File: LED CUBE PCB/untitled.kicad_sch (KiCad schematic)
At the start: 42 parts, among them J1 Conn_01x06, J3 Conn_01x09, SW1 BZCN_TSA007A1518B03, U1 TPS7A2633DRVR, U2 CH340C, Y3 8MHz, Y4 32.786KHz

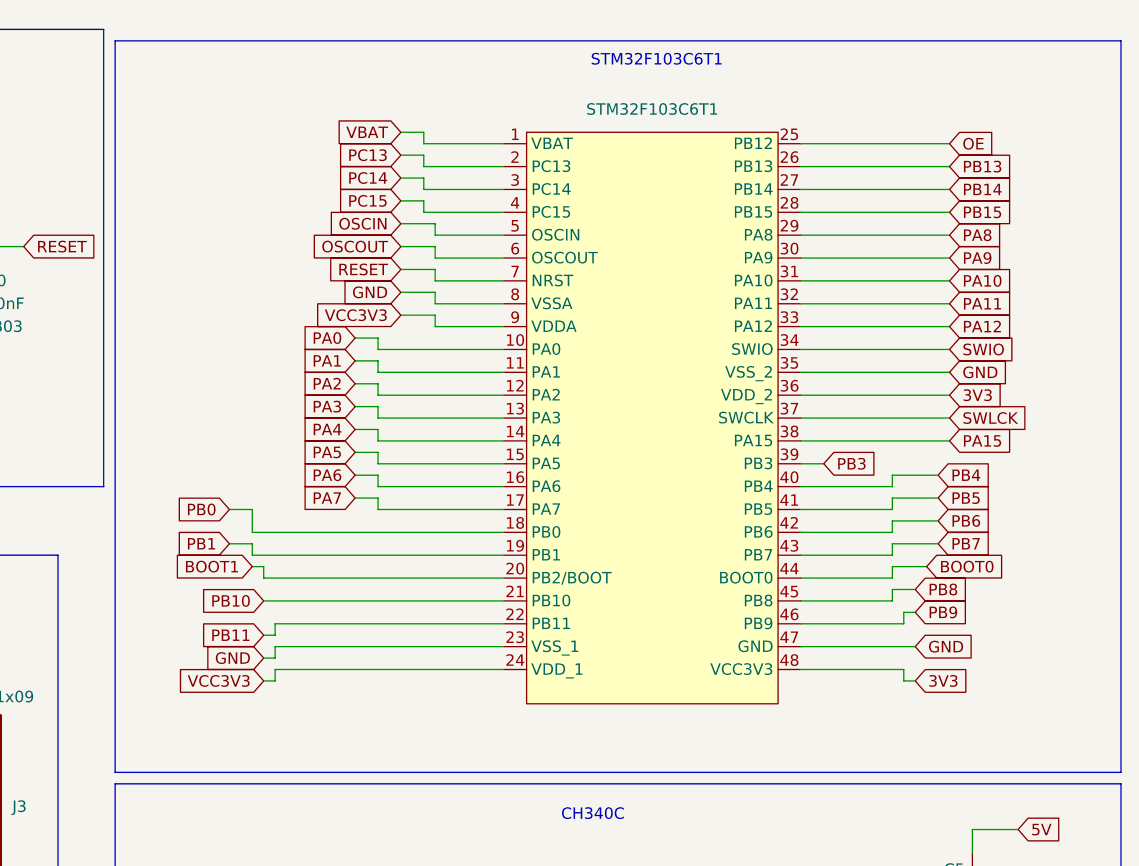
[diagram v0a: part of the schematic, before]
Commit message: Replaced symbol for TXB and STM
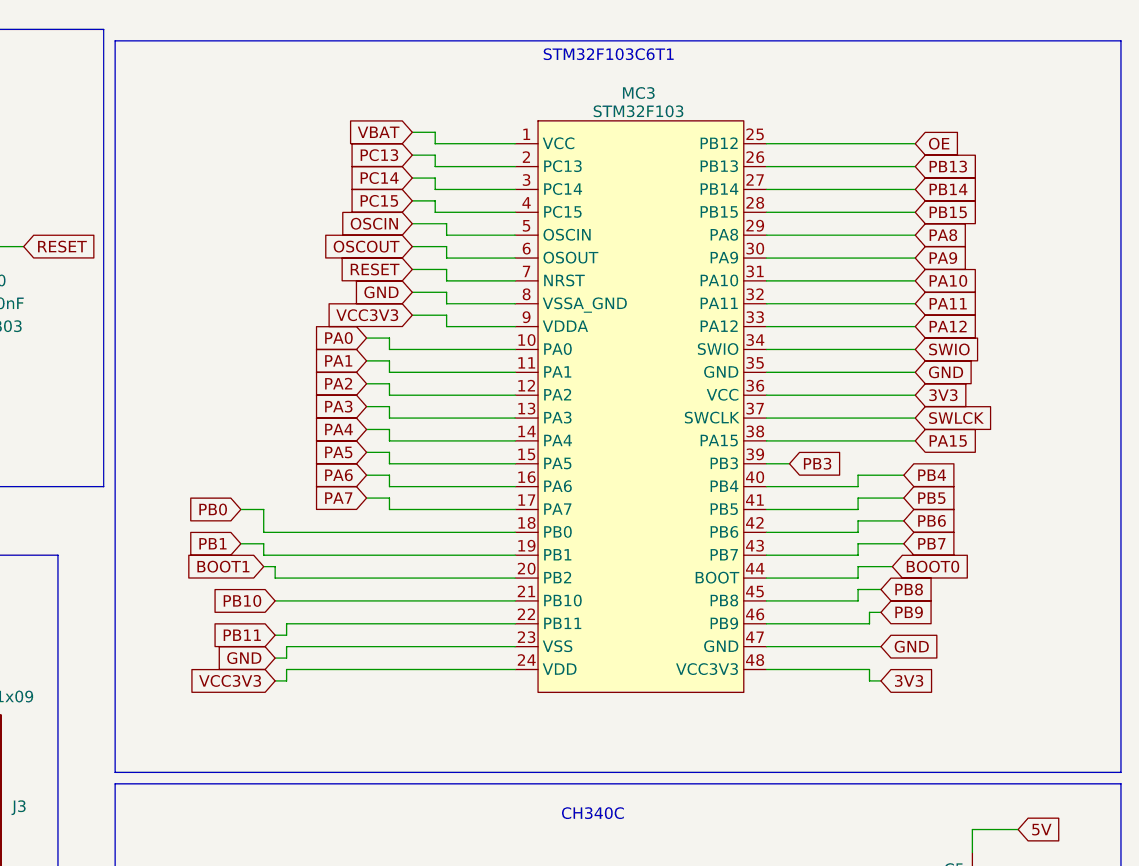
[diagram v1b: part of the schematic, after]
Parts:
- removed STM32F103C6T1: ~, Borna KiCAD Library:TQFP48, symbol STM32F103C6:STM32F103C6
- added MC3: STM32F103, symbol STM32F103c:STM32F103
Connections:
- net 3V3: now also MC3.36 (VCC), MC3.48 (VCC3V3)
- net BOOT0: now also MC3.44 (BOOT)
- net BOOT1: now also MC3.20 (PB2)
- net DN: now also MC3.32 (PA11)
- net DP: now also MC3.33 (PA12)
- net GND: now also MC3.23 (VSS), MC3.35 (GND), MC3.47 (GND), MC3.8 (VSSA_GND)
- net OE: now also MC3.25 (PB12)
- net OSCIN: now also MC3.5 (OSCIN)
- net OSCOUT: now also MC3.6 (OSOUT)
- net PA0: now also MC3.10 (PA0)
- net PA1: now also MC3.11 (PA1)
- net PA10: now also MC3.31 (PA10)
- net PA15: now also MC3.38 (PA15)
- net PA2: now also MC3.12 (PA2)
- net PA3: now also MC3.13 (PA3)
- net PA4: now also MC3.14 (PA4)
- net PA5: now also MC3.15 (PA5)
- net PA6: now also MC3.16 (PA6)
- net PA7: now also MC3.17 (PA7)
- net PA8: now also MC3.29 (PA8)
- net PA9: now also MC3.30 (PA9)
- net PB0: now also MC3.18 (PB0)
- net PB1: now also MC3.19 (PB1)
- net PB10: now also MC3.21 (PB10)
- net PB11: now also MC3.22 (PB11)
- net PB13: now also MC3.26 (PB13)
- net PB14: now also MC3.27 (PB14)
- net PB15: now also MC3.28 (PB15)
- net PB3: now also MC3.39 (PB3)
- net PB4: now also MC3.40 (PB4)
- net PB5: now also MC3.41 (PB5)
- net PB6: now also MC3.42 (PB6)
- net PB7: now also MC3.43 (PB7)
- net PB8: now also MC3.45 (PB8)
- net PB9: now also MC3.46 (PB9)
- net PC13: now also MC3.2 (PC13)
- net PC14: now also MC3.3 (PC14)
- net PC15: now also MC3.4 (PC15)
- net RESET: now also MC3.7 (NRST)
- net SWIO: now also MC3.34 (SWIO)
- net SWLCK: now also MC3.37 (SWCLK)
- net VBAT: now also MC3.1 (VCC)
- net VCC3V3: now also MC3.24 (VDD), MC3.9 (VDDA)

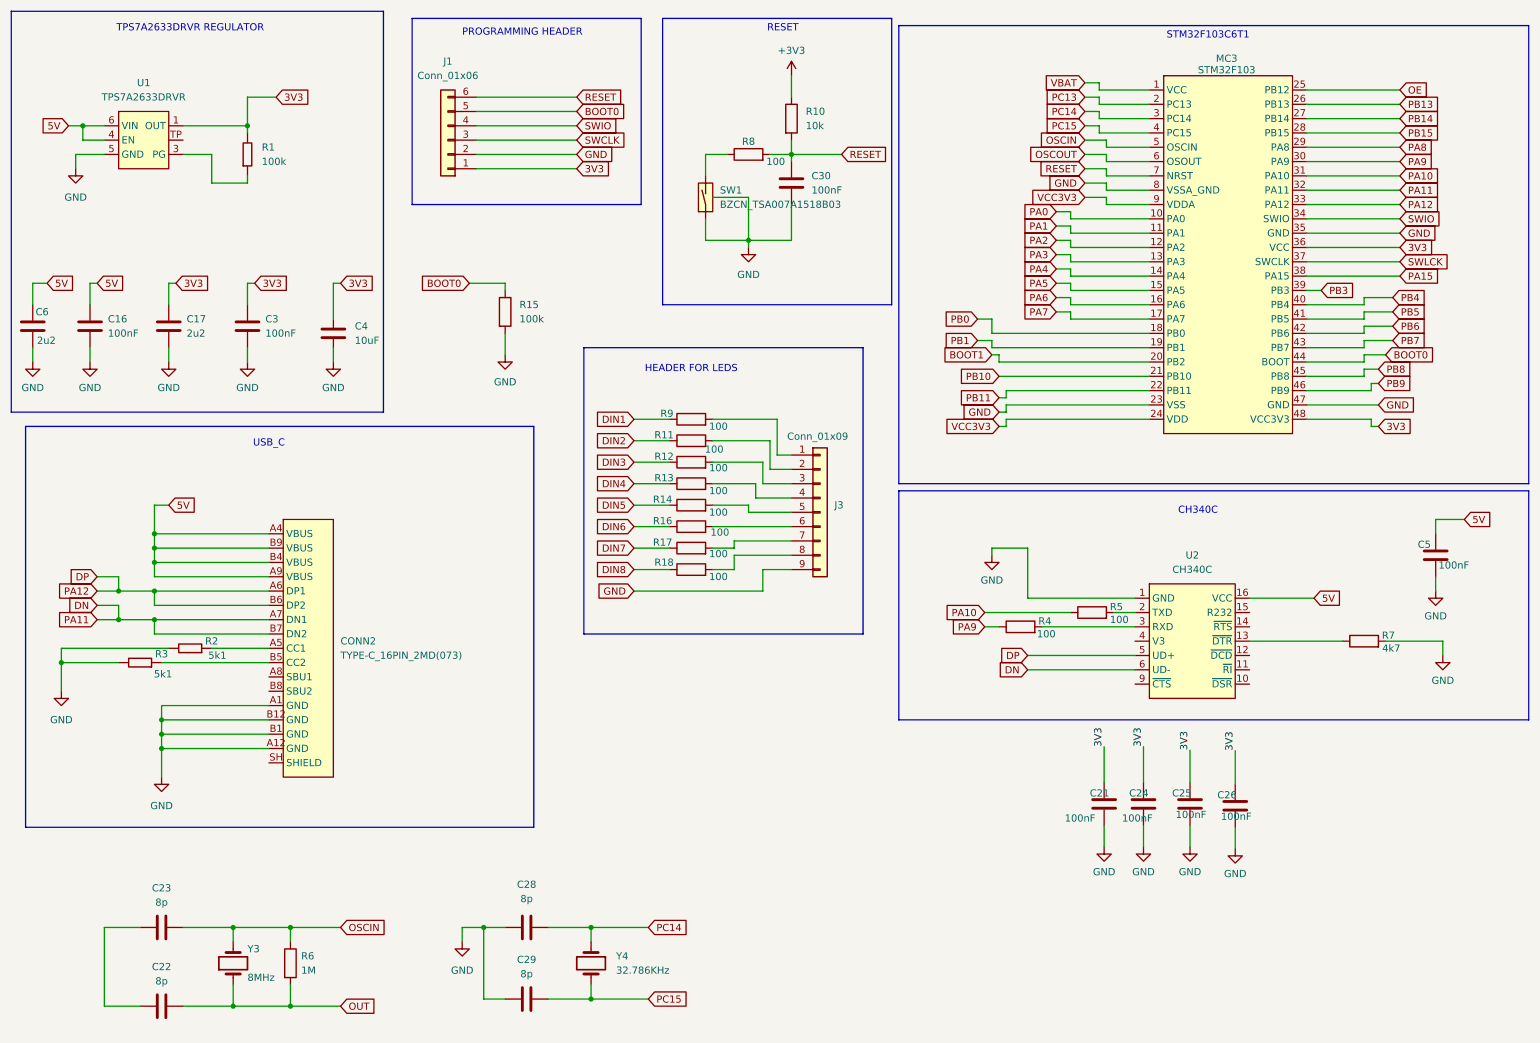
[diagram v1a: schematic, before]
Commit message: Added fuse and bat20
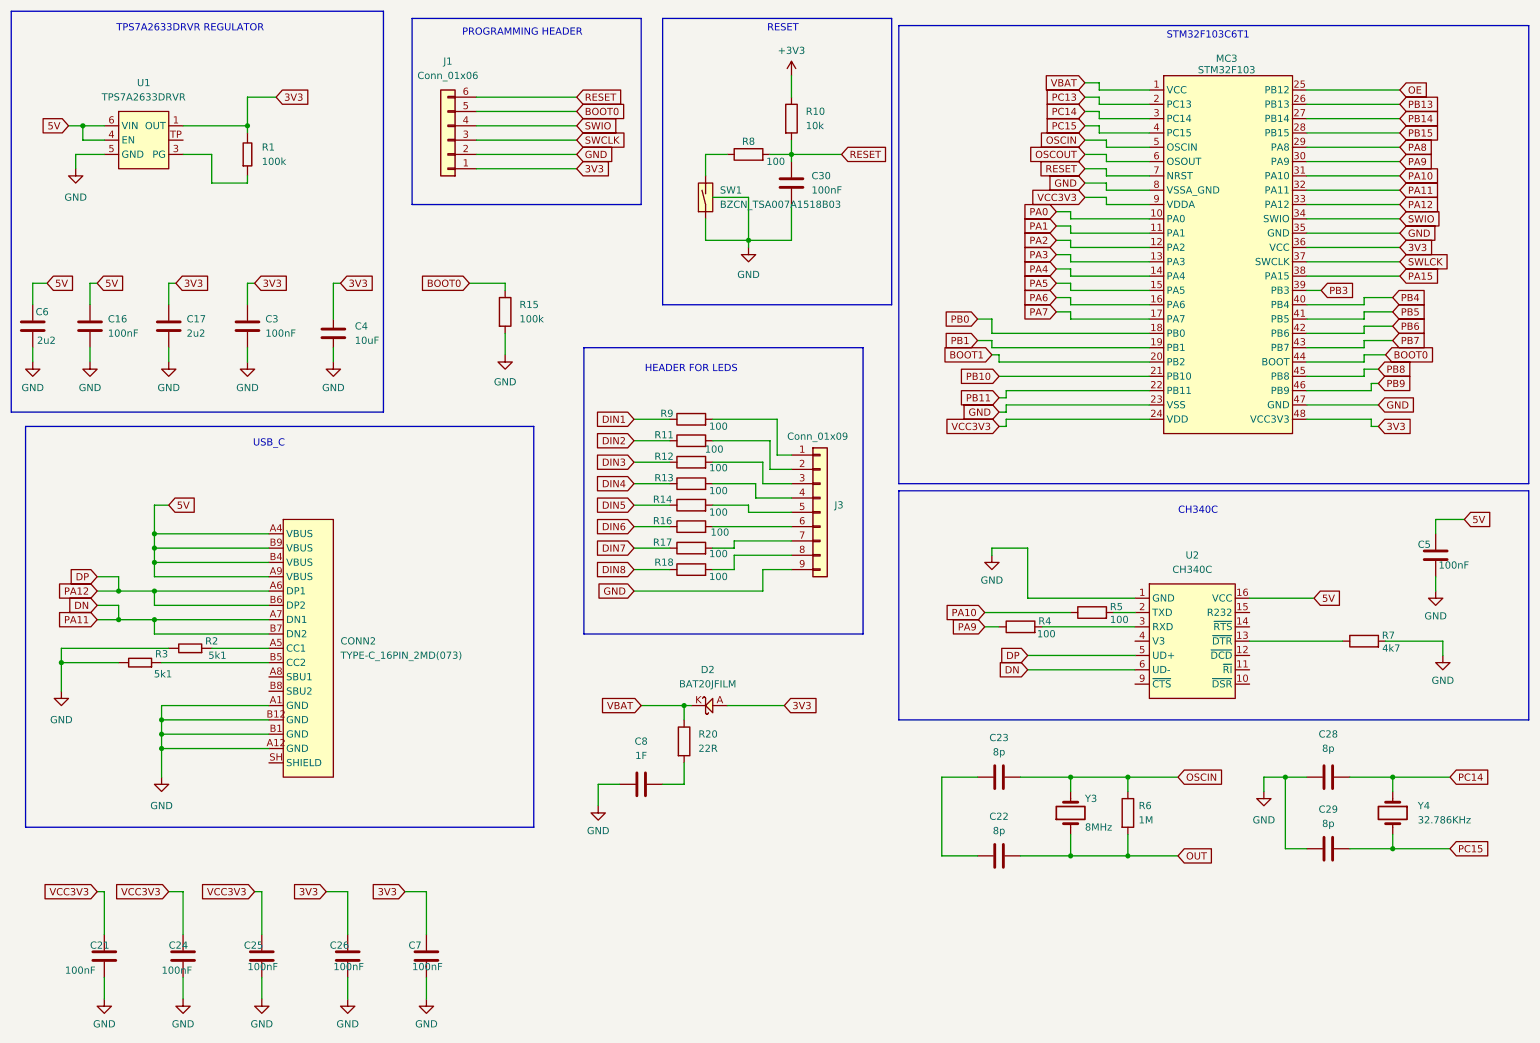
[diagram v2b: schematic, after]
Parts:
- added C7: 100nF, Capacitor_SMD:C_0201_0603Metric_Pad0.64x0.40mm_HandSolder, symbol Device:C
- added C8: 1F, Borna KiCAD Library:C0603, symbol Device:C
- added D2: BAT20JFILM, Borna KiCAD Library:SOD323, symbol Borna KiCAD Library:BAT20JFILM
- added R20: 22R, Borna KiCAD Library:R0603, symbol Device:R
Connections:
- net 3V3: now also C7.1, D2.A; no longer C21.1, C24.1, C25.1
- net GND: now also C7.2, C8.1
- net VBAT: now also D2.K, R20.1
- net VCC3V3: now also C21.1, C24.1, C25.1
- new net: C8.2, R20.2
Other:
- moved on the sheet: C21, C22, C23, C24, C25, C26, C28, C29, R6, Y3, Y4

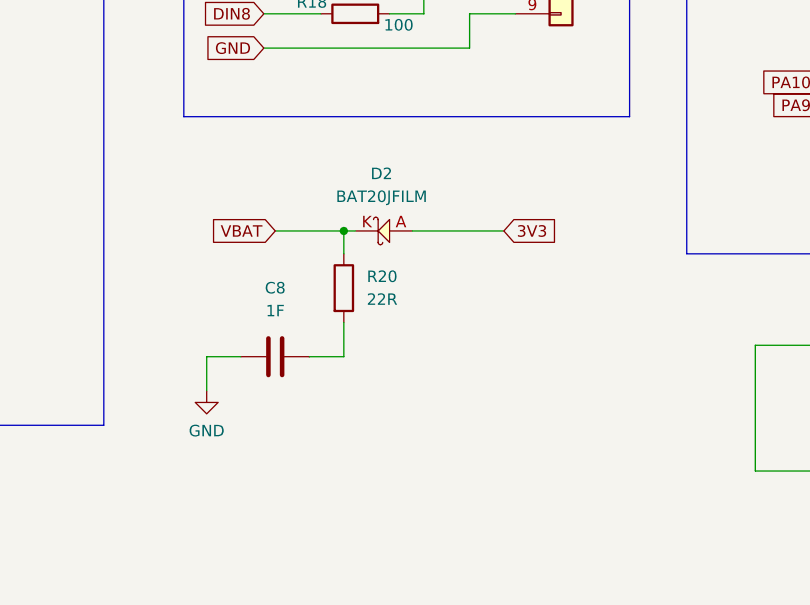
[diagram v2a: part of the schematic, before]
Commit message: Corrected RC filter(Marina)
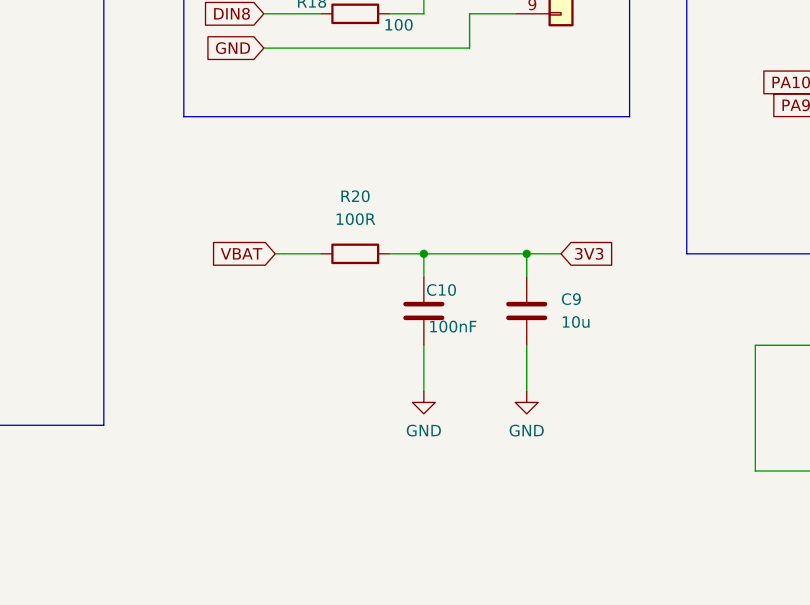
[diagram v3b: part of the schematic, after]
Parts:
- removed C8: 1F, Borna KiCAD Library:C0603, symbol Device:C
- removed D2: BAT20JFILM, Borna KiCAD Library:SOD323, symbol Borna KiCAD Library:BAT20JFILM
- added C10: 100nF, Borna KiCAD Library:C0603, symbol Device:C
- added C9: 10u, Borna KiCAD Library:C0603, symbol Device:C
- C16: footprint Borna KiCAD Library:C0603 -> BornaKiCad:C0603
- MC3: footprint (none) -> BornaKiCad:TQFP48
- R20: value 22R -> 100R
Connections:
- net 3V3: now also R20.2, C10.1, C9.2
- net GND: now also C10.2, C9.1
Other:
- moved on the sheet: R20

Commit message: Schema is finished
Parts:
- C16, C6: footprint BornaKiCad:C0603 -> Borna KiCAD Library:C0603
- C9: footprint Borna KiCAD Library:C0603 -> Borna KiCAD Library:C1206
- MC3: footprint BornaKiCad:TQFP48 -> Borna KiCAD Library:TQFP48
- R11, R12, R13, R14, R15, R16, R17, R18, R8, R9: footprint BornaKiCad:R0603 -> Borna KiCAD Library:R0603
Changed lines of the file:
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@@
 			)
 		)
-		(property "Footprint" "BornaKiCad:R0603"
+		(property "Footprint" "Borna KiCAD Library:R0603"
 			(at 134.62 102.108 90)
 			(effects
@@
 			)
 		)
-		(property "Footprint" "BornaKiCad:R0603"
+		(property "Footprint" "Borna KiCAD Library:R0603"
 			(at 134.62 90.678 90)
 			(effects
@@
 			)
 		)
-		(property "Footprint" "BornaKiCad:R0603"
+		(property "Footprint" "Borna KiCAD Library:R0603"
 			(at 134.62 98.298 90)
 			(effects
@@
 			)
 		)
-		(property "Footprint" "BornaKiCad:R0603"
+		(property "Footprint" "Borna KiCAD Library:R0603"
 			(at 134.62 94.488 90)
 			(effects
@@
 			)
 		)
+		(property "Field5" ""
+			(at 134.62 92.71 90)
+			(effects
+				(font
+					(size 1.27 1.27)
+				)
+				(hide yes)
+			)
+		)
 		(pin "1"
 		)
@@
 			)
 		)
-		(property "Footprint" "BornaKiCad:R0603"
+		(property "Footprint" "Borna KiCAD Library:R0603"
 			(at 134.62 86.868 90)
 			(effects
@@
 			)
 		)
-		(property "Footprint" "Borna KiCAD Library:C0603"
+		(property "Footprint" "Borna KiCAD Library:C1206"
 			(at 152.7048 140.97 0)
 			(effects
@@
 			)
 		)
-		(property "Footprint" "BornaKiCad:C0603"
+		(property "Footprint" "Borna KiCAD Library:C0603"
 			(at 28.9052 72.39 0)
 			(effects
@@
 			)
 		)
-		(property "Footprint" "BornaKiCad:R0603"
+		(property "Footprint" "Borna KiCAD Library:R0603"
 			(at 99.822 66.04 90)
 			(effects
@@
 			)
 		)
-		(property "Footprint" "BornaKiCad:C0603"
+		(property "Footprint" "Borna KiCAD Library:C0603"
 			(at 18.7452 72.39 0)
 			(effects
@@
 			)
 		)
-		(property "Footprint" "BornaKiCad:R0603"
+		(property "Footprint" "Borna KiCAD Library:R0603"
 			(at 144.78 39.878 90)
 			(effects
@@
 			)
 		)
-		(property "Footprint" "BornaKiCad:R0603"
+		(property "Footprint" "Borna KiCAD Library:R0603"
 			(at 134.62 105.918 90)
 			(effects
@@
 			)
 		)
-		(property "Footprint" "BornaKiCad:R0603"
+		(property "Footprint" "Borna KiCAD Library:R0603"
 			(at 134.62 113.538 90)
 			(effects
@@
 			)
 		)
-		(property "Footprint" "BornaKiCad:R0603"
+		(property "Footprint" "Borna KiCAD Library:R0603"
 			(at 134.62 109.728 90)
 			(effects
@@
 			)
 		)
-		(property "Footprint" "BornaKiCad:TQFP48"
+		(property "Footprint" "Borna KiCAD Library:TQFP48"
 			(at 229.87 55.88 0)
 			(effects
